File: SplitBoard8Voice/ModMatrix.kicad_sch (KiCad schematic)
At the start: 96 parts, among them SW501 SB, SW502 MS1, SW503 MD1, SW504 MS2, SW505 MD2, SW506 MS3, SW507 MD3, SW508 MS4, SW509 MD4, SW510 MS5, SW511 MD5, SW512 MS6, SW513 MD6, SW514 MD7, SW515 MD8, U501 MCP23S17_SS

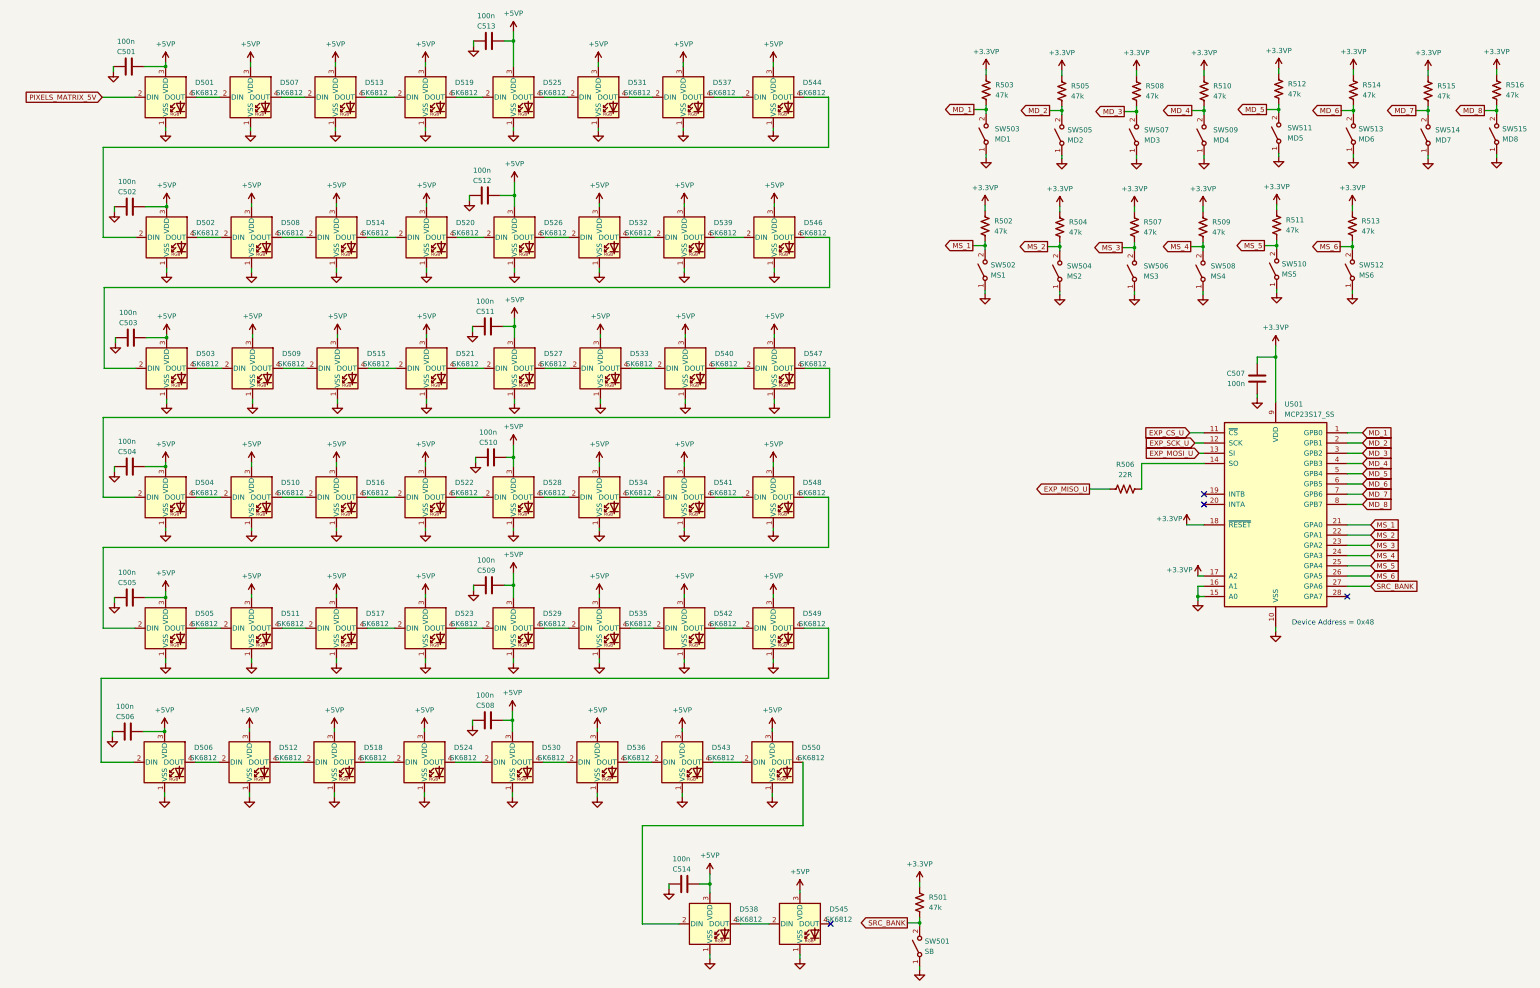
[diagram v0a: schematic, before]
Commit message: back to 3.3v LEDs
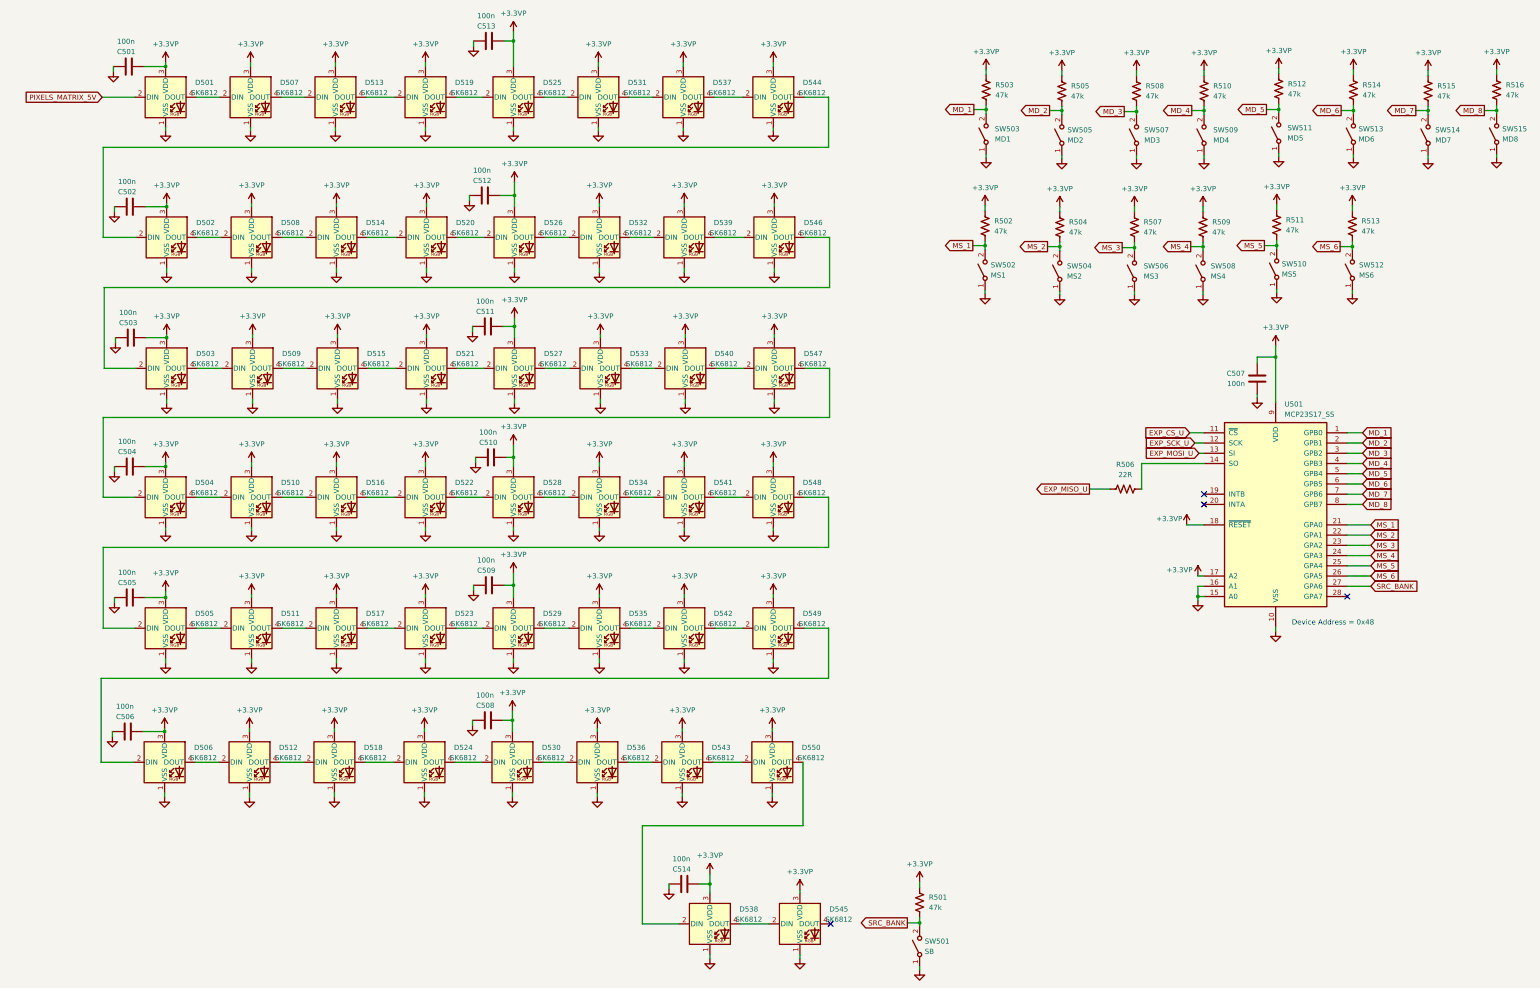
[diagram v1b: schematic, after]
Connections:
- net +5VP is gone; now on net +3.3VP: C501.2, C502.2, C503.2, C504.2, C505.2, C506.2, C508.2, C509.2, C510.2, C511.2, C512.2, C513.2, C514.2, D501.3 (VDD), D502.3 (VDD), D503.3 (VDD), D504.3 (VDD), D505.3 (VDD), D506.3 (VDD), D507.3 (VDD), D508.3 (VDD), D509.3 (VDD), D510.3 (VDD), D511.3 (VDD), D512.3 (VDD), D513.3 (VDD), D514.3 (VDD), D515.3 (VDD), D516.3 (VDD), D517.3 (VDD), D518.3 (VDD), D519.3 (VDD), D520.3 (VDD), D521.3 (VDD), D522.3 (VDD), D523.3 (VDD), D524.3 (VDD), D525.3 (VDD), D526.3 (VDD), D527.3 (VDD), D528.3 (VDD), D529.3 (VDD), D530.3 (VDD), D531.3 (VDD), D532.3 (VDD), D533.3 (VDD), D534.3 (VDD), D535.3 (VDD), D536.3 (VDD), D537.3 (VDD), D538.3 (VDD), D539.3 (VDD), D540.3 (VDD), D541.3 (VDD), D542.3 (VDD), D543.3 (VDD), D544.3 (VDD), D545.3 (VDD), D546.3 (VDD), D547.3 (VDD), D548.3 (VDD), D549.3 (VDD), D550.3 (VDD)

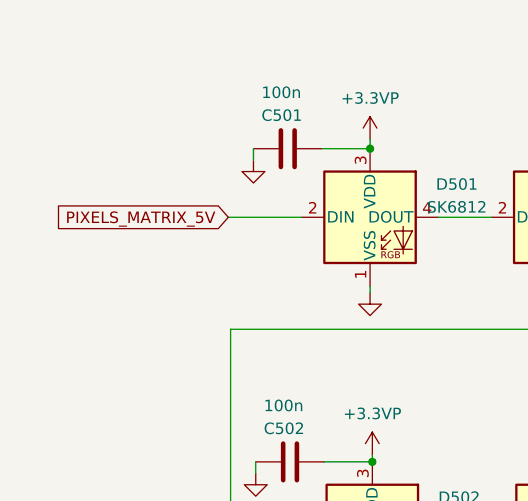
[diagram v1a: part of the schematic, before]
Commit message: upper board routing roughed in
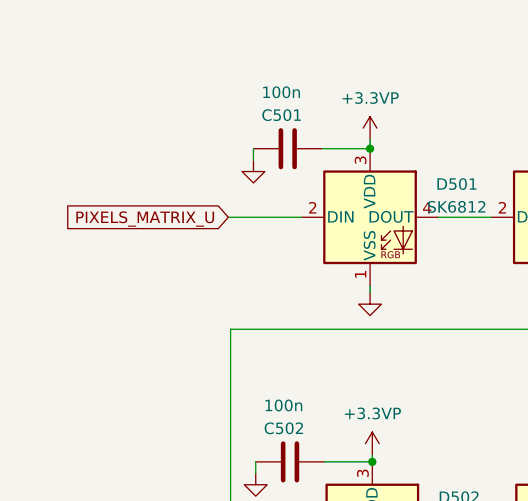
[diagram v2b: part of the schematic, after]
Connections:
- net PIXELS_MATRIX_5V renamed PIXELS_MATRIX_U
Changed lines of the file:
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@@
 		)
 	)
-	(global_label "PIXELS_MATRIX_5V"
+	(global_label "PIXELS_MATRIX_U"
 		(shape input)
 		(at 43.18 42.418 180)
@@
 		)
 		(property "Intersheetrefs" "${INTERSHEET_REFS}"
-			(at 22.8987 42.418 0)
+			(at 23.8663 42.418 0)
 			(effects
 				(font
